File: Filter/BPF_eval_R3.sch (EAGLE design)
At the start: 7 parts, among them U1 885071-A

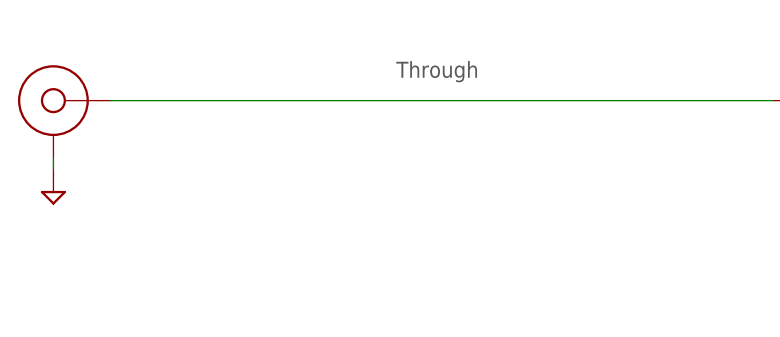
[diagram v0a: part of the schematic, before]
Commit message: Added mounting holes, cleaned up text a bit.
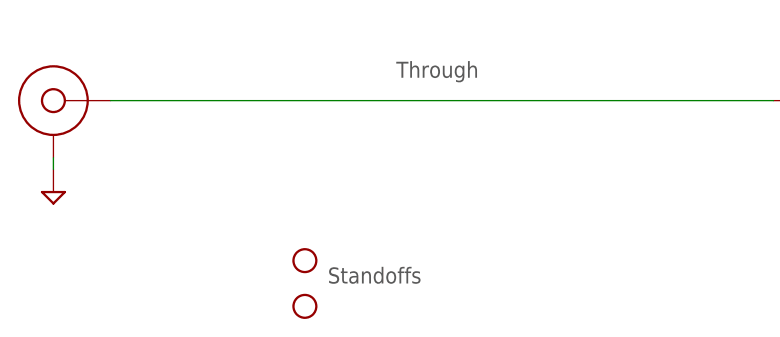
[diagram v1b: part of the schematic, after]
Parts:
- added H1, H2: STAND-OFFTIGHT, SparkFun-Hardware:STAND-OFFTIGHT
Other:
- note added: "Standoffs"
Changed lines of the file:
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@@
 <?xml version="1.0" encoding="utf-8"?>
 <!DOCTYPE eagle SYSTEM "eagle.dtd">
-<eagle version="8.5.0">
+<eagle version="8.5.1">
 <drawing>
 <settings>
@@
 <setting verticaltext="up"/>
 </settings>
-<grid distance="0.05" unitdist="inch" unit="inch" style="lines" multiple="2" display="yes" altdistance="0.01" altunitdist="inch" altunit="inch"/>
+<grid distance="0.1" unitdist="inch" unit="inch" style="lines" multiple="1" display="no" altdistance="0.01" altunitdist="inch" altunit="inch"/>
 <layers>
 <layer number="1" name="Top" color="4" fill="1" visible="no" active="no"/>
@@
 <part name="CF4" library="psas_c3_team05" deviceset="SMA-CINCH-END-FIRE" device=""/>
 <part name="FRAME1" library="frames" library_urn="urn:adsk.eagle:library:229" deviceset="FRAME_A_L" device=""/>
+<part name="H1" library="SparkFun-Hardware" library_urn="urn:adsk.eagle:library:519" deviceset="STAND-OFF" device="TIGHT" package3d_urn="urn:adsk.eagle:package:38629/1"/>
+<part name="H2" library="SparkFun-Hardware" library_urn="urn:adsk.eagle:library:519" deviceset="STAND-OFF" device="TIGHT" package3d_urn="urn:adsk.eagle:package:38629/1"/>
 </parts>
 <sheets>
@@
 <text x="121.92" y="142.24" size="1.778" layer="97">Qorvo 885071-A</text>
 <text x="127" y="101.6" size="1.778" layer="97">Through</text>
+<text x="119.38" y="78.74" size="1.778" layer="97">Standoffs</text>
 </plain>
 <instances>
@@
 <instance part="FRAME1" gate="G$1" x="0" y="0"/>
 <instance part="FRAME1" gate="G$2" x="172.72" y="0"/>
+<instance part="H1" gate="G$1" x="116.84" y="81.28"/>
+<instance part="H2" gate="G$1" x="116.84" y="76.2"/>
 </instances>
 <busses>
@@
 will not be understood (or retained) with this version.
 </note>
+<note version="8.3" severity="warning">
+Since Version 8.3, EAGLE supports the association of 3D packages
+with devices in libraries, schematics, and board files. Those 3D
+packages will not be understood (or retained) with this version.
+</note>
 </compatibility>
